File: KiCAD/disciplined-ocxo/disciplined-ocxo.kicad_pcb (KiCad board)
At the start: 2 copper layers, 159 x 119 mm, 167 parts, among them J1 Conn_02x06_Odd_Even, J2 Conn_Coaxial_Small, J3 Conn_Coaxial_Small, J4 Conn_Coaxial_Small, J5 Conn_Coaxial_Small, Q1 GSFD0650, Q2 GSFD0650, T1 WB1-1L, T2 WB1-1L, T3 WB1-1L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

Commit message: gps PCB 1.1
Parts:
- removed the REF** at (103.0, 122.2)
- R8: value R -> 910

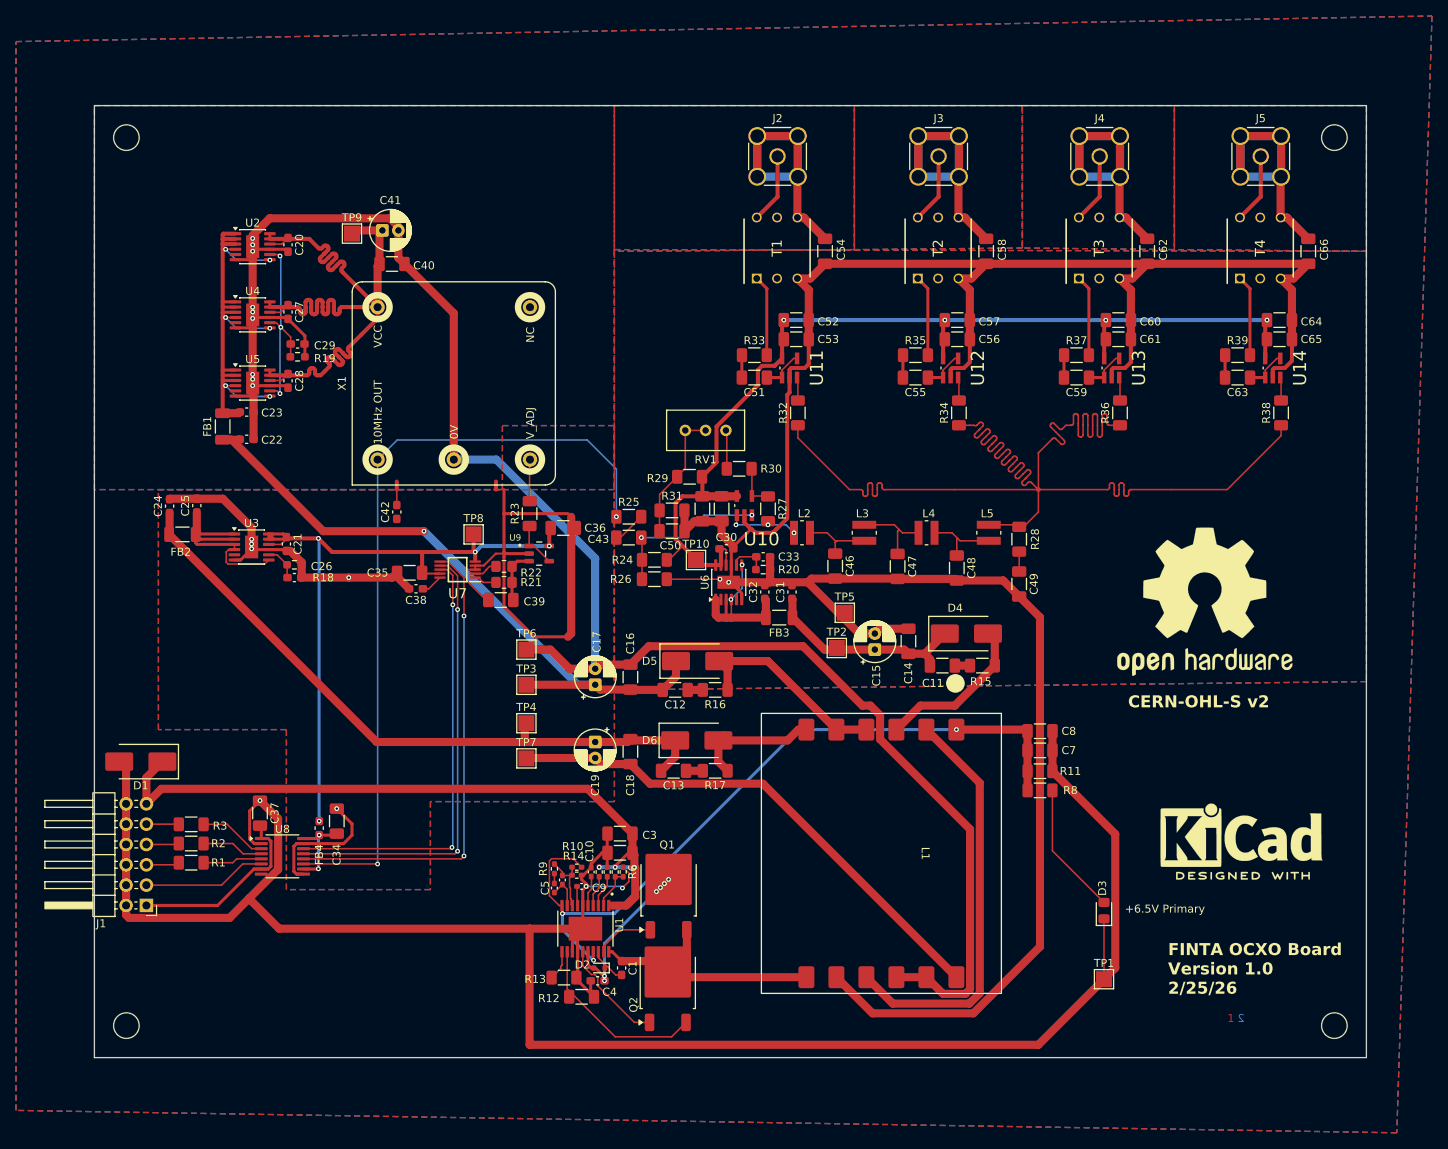
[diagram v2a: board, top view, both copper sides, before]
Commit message: ocxo board 1.1, with fixes for the major errors
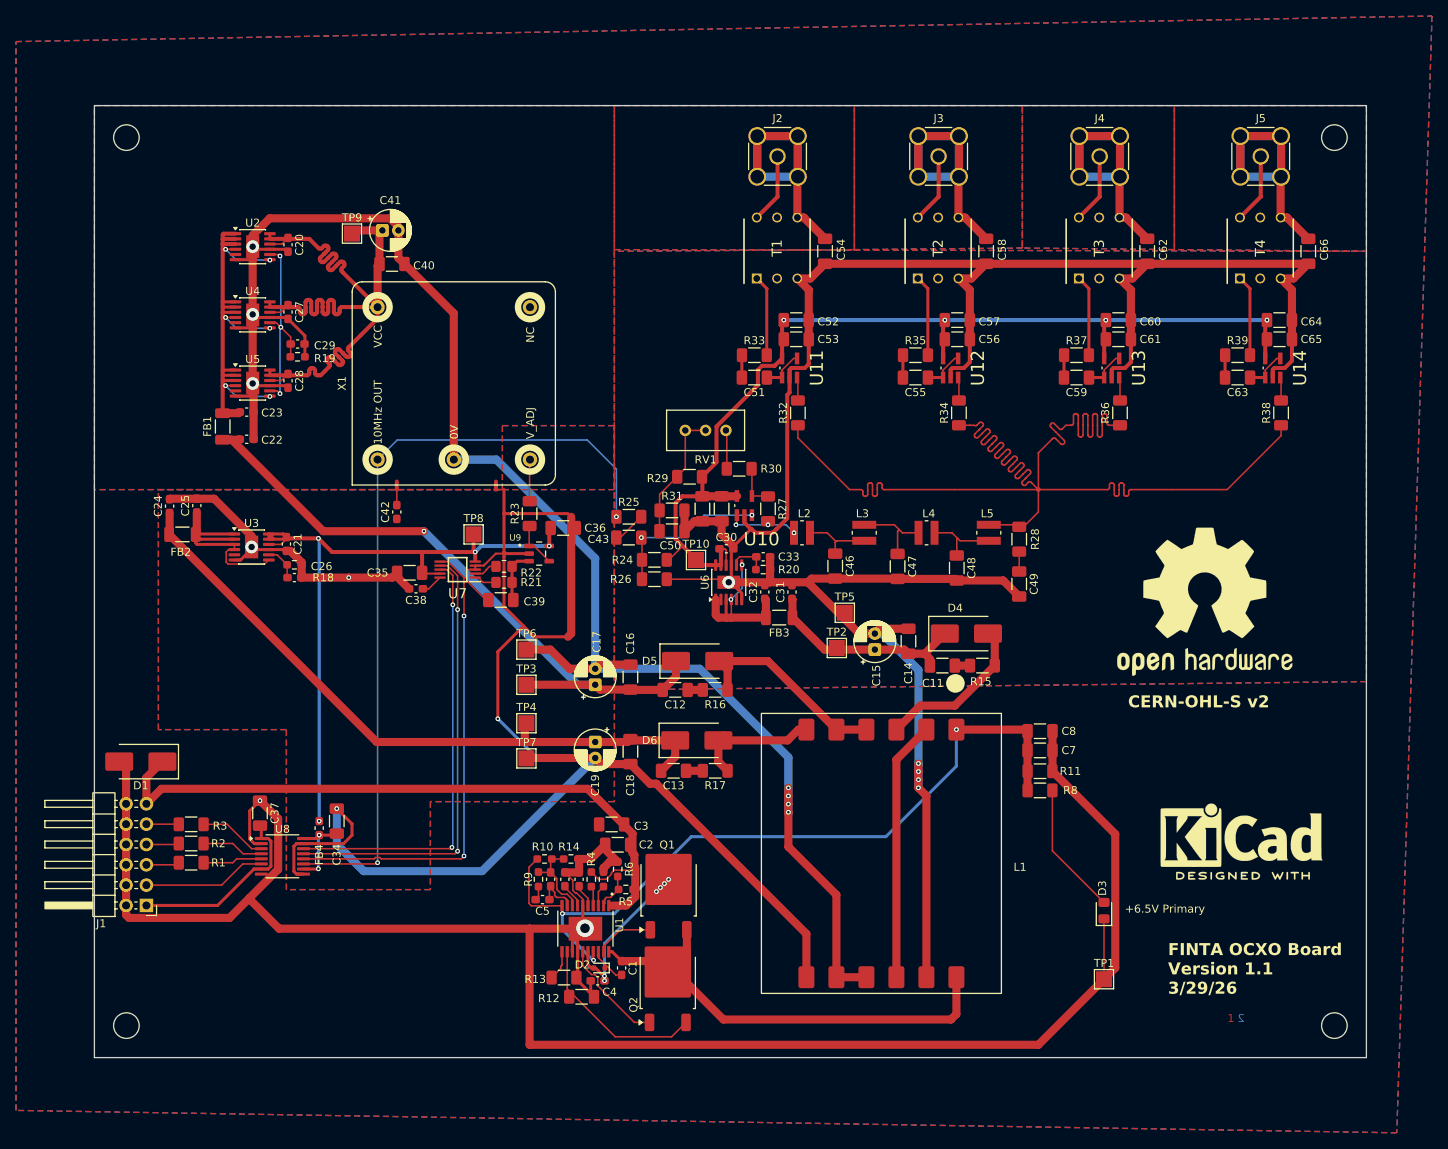
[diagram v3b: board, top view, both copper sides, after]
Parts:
- C10, C5, C6, C9: footprint Capacitor_SMD:C_0402_1005Metric_Pad0.74x0.62mm_HandSolder -> Capacitor_SMD:C_0603_1608Metric_Pad1.08x0.95mm_HandSolder
- R10: value 50K -> 51K; footprint Resistor_SMD:R_0402_1005Metric_Pad0.72x0.64mm_HandSolder -> Resistor_SMD:R_0603_1608Metric_Pad0.98x0.95mm_HandSolder
- R14: value 11.5K -> 12K; footprint Resistor_SMD:R_0402_1005Metric_Pad0.72x0.64mm_HandSolder -> Resistor_SMD:R_0603_1608Metric_Pad0.98x0.95mm_HandSolder
- R4: footprint Resistor_SMD:R_0402_1005Metric_Pad0.72x0.64mm_HandSolder -> Resistor_SMD:R_0603_1608Metric_Pad0.98x0.95mm_HandSolder
- R5: value 15.4K -> 15K; footprint Resistor_SMD:R_0402_1005Metric_Pad0.72x0.64mm_HandSolder -> Resistor_SMD:R_0603_1608Metric_Pad0.98x0.95mm_HandSolder
- R6: value 2.26K -> 2.4K; footprint Resistor_SMD:R_0402_1005Metric_Pad0.72x0.64mm_HandSolder -> Resistor_SMD:R_0603_1608Metric_Pad0.98x0.95mm_HandSolder
- R7: value 25K -> 24K; footprint Resistor_SMD:R_0402_1005Metric_Pad0.72x0.64mm_HandSolder -> Resistor_SMD:R_0603_1608Metric_Pad0.98x0.95mm_HandSolder
- R9: value 210K -> 200K; footprint Resistor_SMD:R_0402_1005Metric_Pad0.72x0.64mm_HandSolder -> Resistor_SMD:R_0603_1608Metric_Pad0.98x0.95mm_HandSolder
- moved R10 4.16 mm to (128.3, 106.2), turned to 180 degrees
- moved R5 2.56 mm to (138.4, 110.0), turned to 0 degrees
- moved R9 2.39 mm to (127.5, 108.7)
- moved C9 2.27 mm to (130.8, 108.7), turned to 90 degrees
- moved R14 2.15 mm to (131.6, 106.2)
- moved C5 2.08 mm to (128.0, 111.3), turned to 180 degrees
- moved C10 1.77 mm to (132.6, 108.7)
- moved C3 1.55 mm to (136.7, 101.9)
- moved C6 1.47 mm to (129.0, 108.7)
- moved R4 1.34 mm to (134.1, 108.7)
- moved C2 1.05 mm to (137.4, 104.4)
- moved R7 1.02 mm to (135.6, 108.7)
- moved R6 0.77 mm to (137.4, 107.4)
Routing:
- net /ocxo/6V Analog GND Isolated: track 185.4 -> 240.4 mm, vias 5 -> 4
- net /pre-reg power/SW: track 34.6 -> 62.0 mm
- net /distribution/Analog GND: track 323.8 -> 297.4 mm, vias 2 -> 5
- net Net-(L1-Pad10): track 51.8 -> 32.5 mm
- net /ocxo/6V OVEN GND Isolated: track 238.9 -> 219.7 mm, vias 9 -> 7
- net GND: track 273.1 -> 270.3 mm, vias 3 -> 2
- net /pre-reg power/FB: track 8.13 -> 10.4 mm
- net Net-(D2-A): track 20.8 -> 22.9 mm
- net /pre-reg power/6.5v switcher: track 95.7 -> 97.7 mm
- net /pre-reg power/EN: track 3.91 -> 2.47 mm
- net Net-(U1-RT/SYNC): track 4.06 -> 2.64 mm
- net /pre-reg power/COMP: track 4.30 -> 5.37 mm
- net /pre-reg power/RAMP: track 3.83 -> 2.89 mm
- net /pre-reg power/12V IN: track 88.6 -> 87.7 mm, vias 3 -> 0
- net /pre-reg power/SS: track 2.43 -> 3.08 mm
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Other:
- board text added: "FINTA OCXO Board Version 1.1 3/29/26"
- board text removed: "FINTA OCXO Board Version 1.0 2/25/26"

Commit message: OCXO board 1.1
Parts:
- added FID1: Fiducial, Fiducial:Fiducial_1mm_Mask3mm, F.Cu at (75.1, 23.0)
- added FID2: Fiducial, Fiducial:Fiducial_1mm_Mask3mm, F.Cu at (226.8, 24.1)
- added FID3: Fiducial, Fiducial:Fiducial_1mm_Mask3mm, F.Cu at (83.4, 126.9)
- C35, C36, C37, C40: footprint Capacitor_SMD:C_1206_3216Metric_Pad1.33x1.80mm_HandSolder -> Capacitor_SMD:C_0603_1608Metric_Pad1.08x0.95mm_HandSolder
